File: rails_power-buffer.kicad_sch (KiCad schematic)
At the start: 4 parts

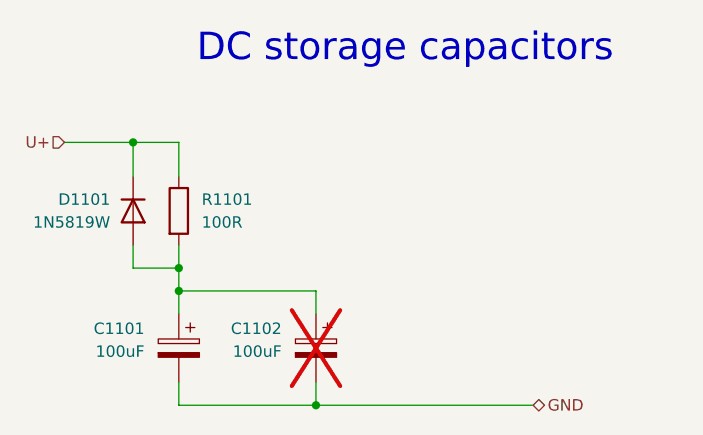
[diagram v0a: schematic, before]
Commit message: Fix - revert to working model
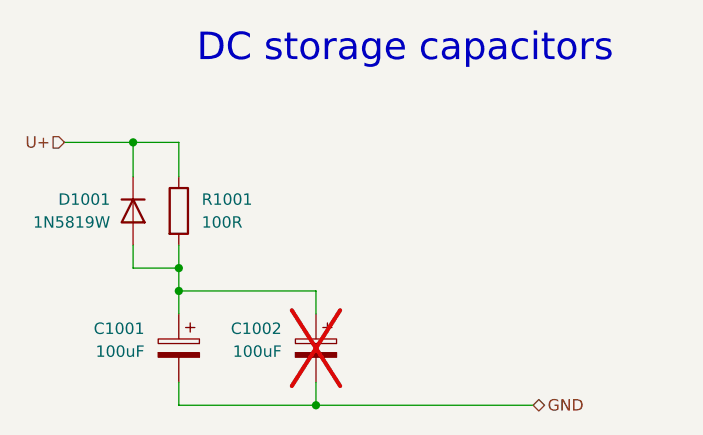
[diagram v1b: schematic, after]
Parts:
- renumbered C1101 to C1001, C1102 to C1002, D1101 to D1001, R1101 to R1001
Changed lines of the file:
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@@
 		(dnp no)
 		(fields_autoplaced yes)
-		(property "Reference" "C1101"
+		(property "Reference" "C1001"
 			(at 33.02 58.801 0)
 			(effects
@@
 			(project "xDuinoRails-Thor-M"
 				(path "/fb33ec4e-6596-45d2-a121-8d3475acd69a/0bf87bfc-1a64-4ae3-9476-ab62edd28dcb"
-					(reference "C1101")
+					(reference "C1001")
 					(unit 1)
 				)
@@
 		(dnp yes)
 		(fields_autoplaced yes)
-		(property "Reference" "C1102"
+		(property "Reference" "C1002"
 			(at 48.26 58.801 0)
 			(effects
@@
 			(project "xDuinoRails-Thor-M"
 				(path "/fb33ec4e-6596-45d2-a121-8d3475acd69a/0bf87bfc-1a64-4ae3-9476-ab62edd28dcb"
-					(reference "C1102")
+					(reference "C1002")
 					(unit 1)
 				)
@@
 		(dnp no)
 		(fields_autoplaced yes)
-		(property "Reference" "R1101"
+		(property "Reference" "R1001"
 			(at 39.37 44.4499 0)
 			(effects
@@
 			(project ""
 				(path "/fb33ec4e-6596-45d2-a121-8d3475acd69a/0bf87bfc-1a64-4ae3-9476-ab62edd28dcb"
-					(reference "R1101")
+					(reference "R1001")
 					(unit 1)
 				)
@@
 		(on_board yes)
 		(dnp no)
-		(property "Reference" "D1101"
+		(property "Reference" "D1001"
 			(at 29.21 44.4499 90)
 			(effects
@@
 			(project ""
 				(path "/fb33ec4e-6596-45d2-a121-8d3475acd69a/0bf87bfc-1a64-4ae3-9476-ab62edd28dcb"
-					(reference "D1101")
+					(reference "D1001")
 					(unit 1)
 				)

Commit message: Fix - Remove ERC error, refresh annotation
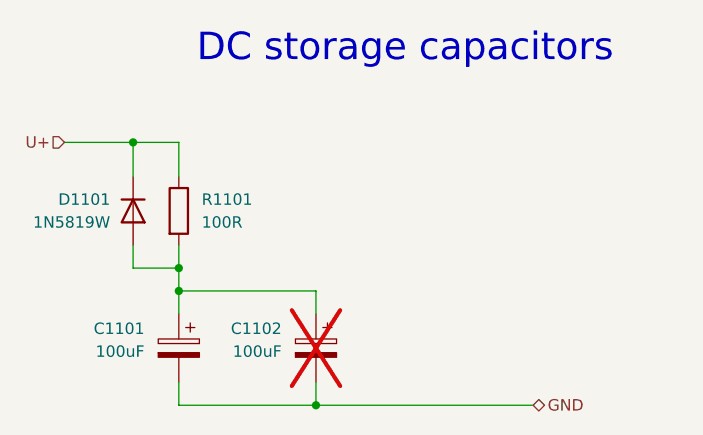
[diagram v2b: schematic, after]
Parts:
- renumbered C1001 to C1101, C1002 to C1102, D1001 to D1101, R1001 to R1101
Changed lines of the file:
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@@
 		(dnp no)
 		(fields_autoplaced yes)
-		(property "Reference" "C1001"
+		(property "Reference" "C1101"
 			(at 33.02 58.801 0)
 			(effects
@@
 			(project "xDuinoRails-Thor-M"
 				(path "/fb33ec4e-6596-45d2-a121-8d3475acd69a/0bf87bfc-1a64-4ae3-9476-ab62edd28dcb"
-					(reference "C1001")
+					(reference "C1101")
 					(unit 1)
 				)
@@
 		(dnp yes)
 		(fields_autoplaced yes)
-		(property "Reference" "C1002"
+		(property "Reference" "C1102"
 			(at 48.26 58.801 0)
 			(effects
@@
 			(project "xDuinoRails-Thor-M"
 				(path "/fb33ec4e-6596-45d2-a121-8d3475acd69a/0bf87bfc-1a64-4ae3-9476-ab62edd28dcb"
-					(reference "C1002")
+					(reference "C1102")
 					(unit 1)
 				)
@@
 		(dnp no)
 		(fields_autoplaced yes)
-		(property "Reference" "R1001"
+		(property "Reference" "R1101"
 			(at 39.37 44.4499 0)
 			(effects
@@
 			(project ""
 				(path "/fb33ec4e-6596-45d2-a121-8d3475acd69a/0bf87bfc-1a64-4ae3-9476-ab62edd28dcb"
-					(reference "R1001")
+					(reference "R1101")
 					(unit 1)
 				)
@@
 		(on_board yes)
 		(dnp no)
-		(property "Reference" "D1001"
+		(property "Reference" "D1101"
 			(at 29.21 44.4499 90)
 			(effects
@@
 			(project ""
 				(path "/fb33ec4e-6596-45d2-a121-8d3475acd69a/0bf87bfc-1a64-4ae3-9476-ab62edd28dcb"
-					(reference "D1001")
+					(reference "D1101")
 					(unit 1)
 				)
